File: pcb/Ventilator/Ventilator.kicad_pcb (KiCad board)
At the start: 2 copper layers, 68 parts, among them J1 Screw_Terminal_01x08, J2 Screw_Terminal_01x02, J3 Screw_Terminal_01x08, K1 FINDER-40.52.7.012.0000, K2 FINDER-40.52.7.012.0000, K3 FINDER-40.52.7.012.0000, Q1 NUD3160, Q2 NUD3160, Q3 NUD3160, SW1 Reset, U1 4N25, U2 4N25, U3 4N25, U4 4N25

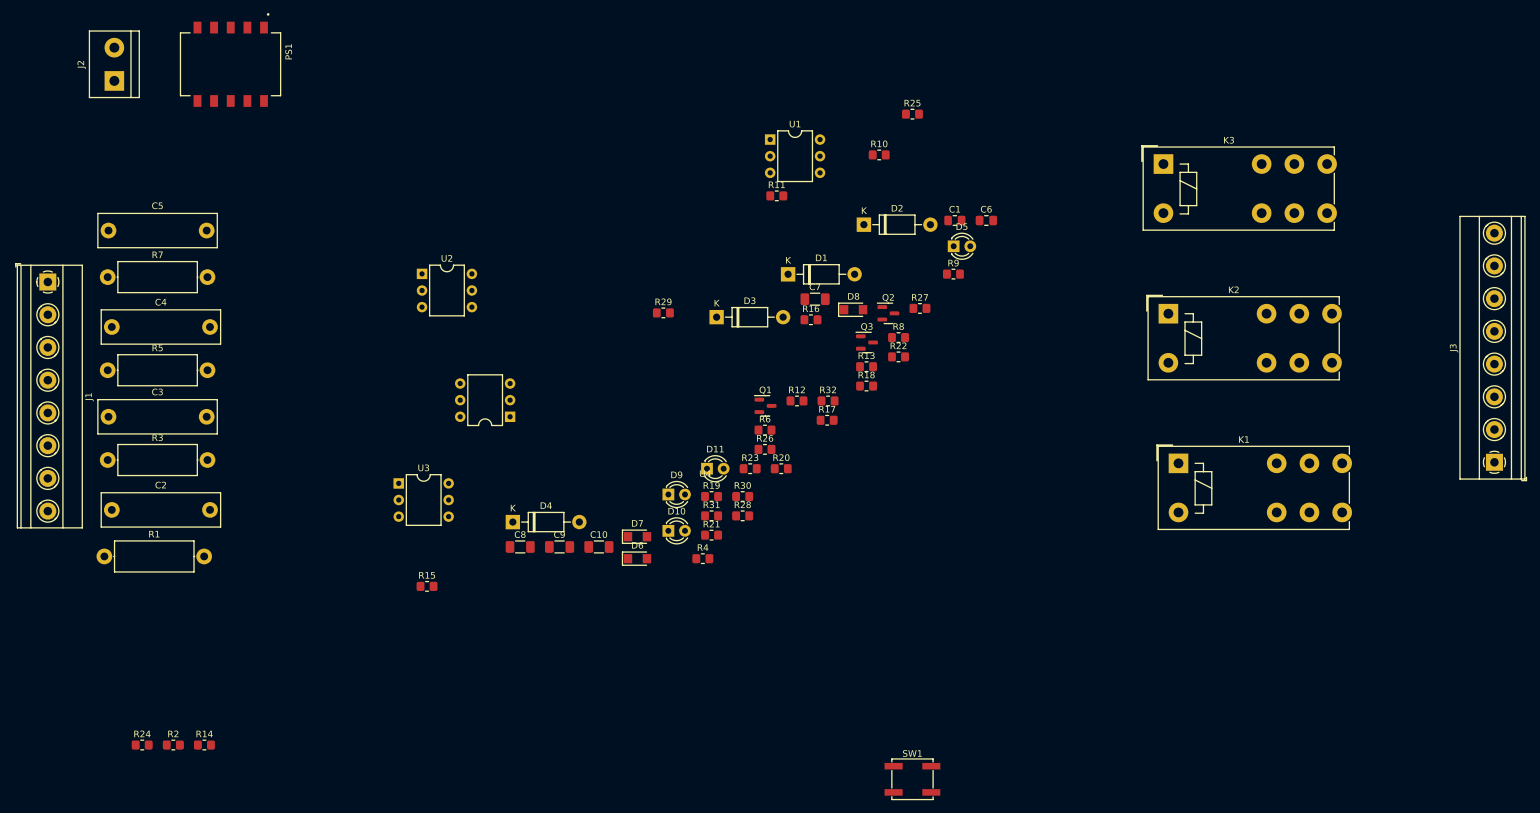
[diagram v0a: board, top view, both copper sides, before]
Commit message: -components placed
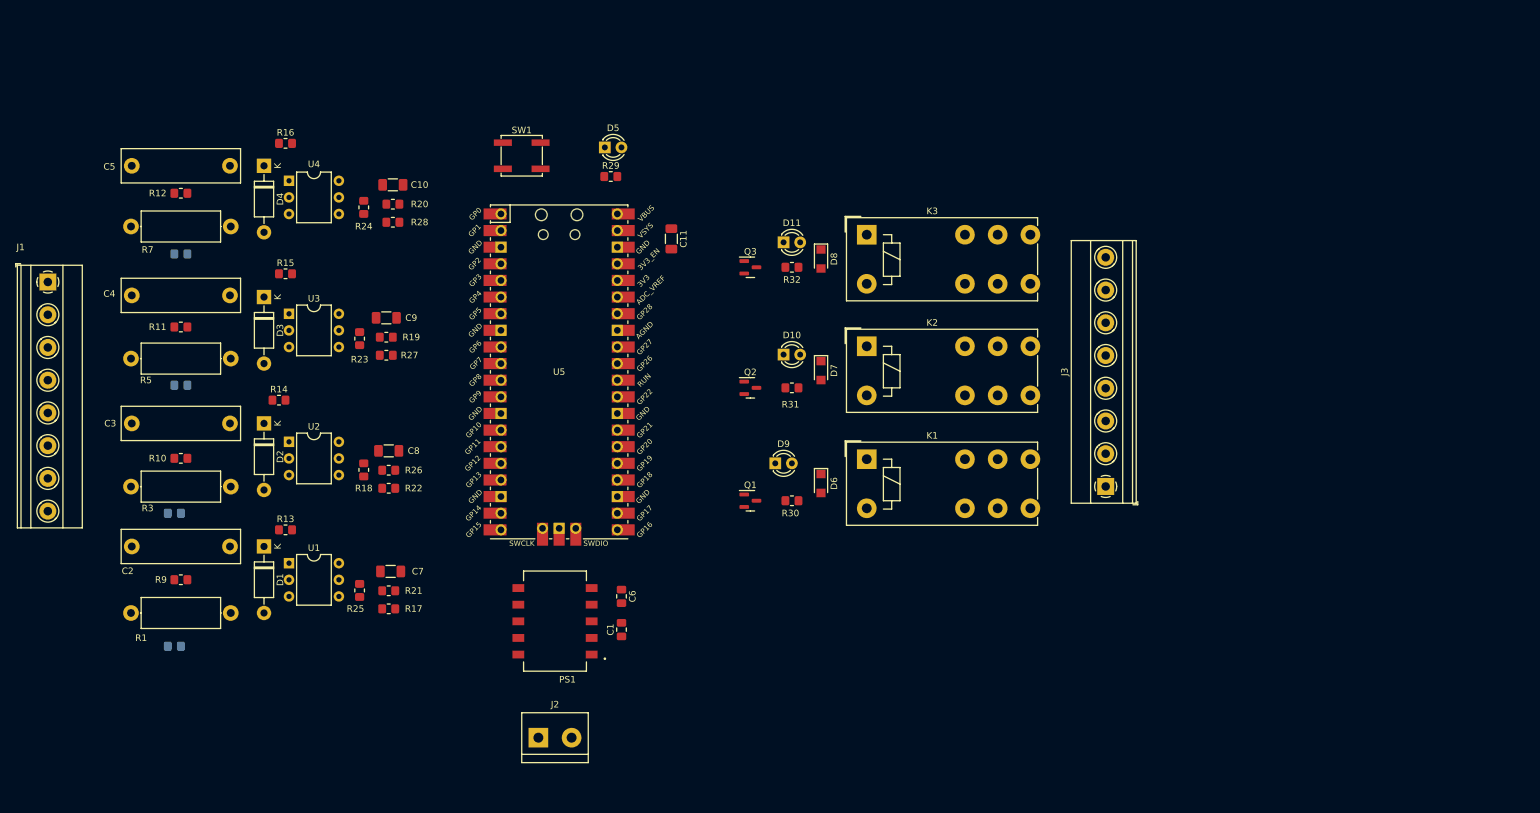
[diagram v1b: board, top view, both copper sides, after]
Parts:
- added C11: 100n, Capacitor_SMD:C_1206_3216Metric_Pad1.33x1.80mm_HandSolder, F.Cu at (118.1, 67.3)
- added U5: Pico, MCU_RaspberryPi_and_Boards:RPi_Pico_SMD_TH, F.Cu at (101.0, 87.6)
- R2, R4, R6, R8: moved to B.Cu
- moved R9 126.9 mm to (43.2, 119.4), turned to 180 degrees
- moved J2 119.4 mm to (97.8, 143.5), turned to 0 degrees
- moved R10 116.3 mm to (43.2, 100.8), turned to 180 degrees
- moved SW1 112.4 mm to (95.2, 54.6)
- moved R25 111.5 mm to (70.5, 121.0), turned to 90 degrees
- moved R8 110.4 mm to (43.2, 69.6)
- moved R12 99.3 mm to (43.2, 60.3), turned to 180 degrees
- moved PS1 98.5 mm to (100.3, 125.7), turned to 180 degrees
- moved U1 97.9 mm to (59.7, 116.9)
- moved D2 96.5 mm to (55.9, 95.5), turned to -90 degrees
- moved R11 93.2 mm to (43.2, 80.8), turned to 180 degrees
- moved R13 92.2 mm to (59.2, 111.8)
- moved D1 90.2 mm to (55.9, 114.3), turned to -90 degrees
- moved R6 89.5 mm to (43.2, 89.7)
- moved R24 88.8 mm to (71.1, 62.5), turned to 90 degrees
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
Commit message: - as send to JCLPCB
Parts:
- added TP1: TestPoint, TestPoint:TestPoint_Bridge_Pitch2.54mm_Drill1.0mm, F.Cu at (77.5, 127.0)
- added TP2: TestPoint, TestPoint:TestPoint_Bridge_Pitch2.54mm_Drill1.0mm, F.Cu at (77.5, 108.2)
- added TP3: TestPoint, TestPoint:TestPoint_Bridge_Pitch2.54mm_Drill1.0mm, F.Cu at (77.5, 88.4)
- added TP4: TestPoint, TestPoint:TestPoint_Bridge_Pitch2.54mm_Drill1.0mm, F.Cu at (77.5, 68.1)
- moved J2 17.8 mm to (82.8, 133.9)
- moved R25 5.38 mm to (75.1, 123.8), turned to 0 degrees
- moved R22 5.18 mm to (70.7, 102.4), turned to 90 degrees
- moved R21 4.57 mm to (70.4, 120.9), turned to 90 degrees
- moved R18 3.82 mm to (74.9, 102.4), turned to 0 degrees
- moved R17 2.80 mm to (75.1, 121.0)
- moved R26 2.50 mm to (74.9, 105.2)
- moved D9 1.37 mm to (135.1, 102.4)
- moved C7 0.15 mm to (75.1, 118.1)
- turned C8 to 0 degrees
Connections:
- net Net-(R27-Pad2) renamed /IN3
- R25 pad 2: Net-(R25-Pad2) -> /IN1
- R26 pad 2: Net-(R26-Pad2) -> /IN2
- R28 pad 2: Net-(R28-Pad2) -> /IN4
- U5 pad 1: Net-(R25-Pad2) -> Net-(D5-Pad1)
- U5 pad 19: unconnected-(U5-Pad19) -> /IN2
- U5 pad 2: Net-(R26-Pad2) -> /IN4
- U5 pad 20: unconnected-(U5-Pad20) -> /IN1
- U5 pad 21: Net-(Q3-Pad1) -> unconnected-(U5-Pad21)
- U5 pad 22: Net-(Q2-Pad1) -> unconnected-(U5-Pad22)
- U5 pad 29: unconnected-(U5-Pad29) -> Net-(Q2-Pad1)
- U5 pad 34: unconnected-(U5-Pad34) -> Net-(Q3-Pad1)
- U5 pad 5: Net-(R28-Pad2) -> unconnected-(U5-Pad5)
- U5 pad 6: Net-(D5-Pad1) -> unconnected-(U5-Pad6)
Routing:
- net VCC: track 0.00 -> 328.8 mm, vias 0 -> 3
- net Net-(SW1-Pad2): track 0.00 -> 56.0 mm, vias 0 -> 2
- net Net-(R2-Pad1): track 0.00 -> 36.1 mm
- net /IN3: track 0.00 -> 31.6 mm
- net Net-(R4-Pad1): track 0.00 -> 28.8 mm
- net /IN1: track 0.00 -> 27.3 mm
- net Net-(J3-Pad6): track 0.00 -> 27.2 mm
- net Net-(C1-Pad1): track 0.00 -> 26.5 mm
- net /IN2: track 0.00 -> 24.1 mm
- net Net-(Q3-Pad1): track 0.00 -> 22.8 mm
- net Net-(R7-Pad1): track 0.00 -> 22.7 mm
- net Net-(D6-Pad2): track 0.00 -> 22.7 mm
- net Net-(D2-Pad2): track 0.00 -> 22.4 mm
- net /IN4: track 0.00 -> 22.3 mm
- net Net-(R6-Pad1): track 0.00 -> 21.8 mm
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- added copper zone on B.Cu, net GND
- added copper zone on F.Cu, net GND
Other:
- board outline added: 172.7 x 91.4 mm

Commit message: - added rp2040, multiple sheets, etc...
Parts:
- removed J1: Screw_Terminal_01x08, TerminalBlock_Phoenix:TerminalBlock_Phoenix_MKDS-1,5-8_1x08_P5.00mm_Horizontal
- removed R1: 2.2k, Resistor_THT:R_Axial_DIN0414_L11.9mm_D4.5mm_P15.24mm_Horizontal
- removed R2: 100R, Resistor_SMD:R_0805_2012Metric_Pad1.20x1.40mm_HandSolder
- added C12: 100n, Capacitor_SMD:C_1206_3216Metric_Pad1.33x1.80mm_HandSolder, F.Cu at (158.6, 138.7)
- added C13: 100n, Capacitor_SMD:C_1206_3216Metric_Pad1.33x1.80mm_HandSolder, F.Cu at (158.6, 142.0)
- added C14: 100n, Capacitor_SMD:C_1206_3216Metric_Pad1.33x1.80mm_HandSolder, F.Cu at (170.6, 135.3)
- added C15: 0.1u, Capacitor_THT:C_Rect_L18.0mm_W5.0mm_P15.00mm_FKS3_FKP3, F.Cu at (83.0, 84.5)
- added C16: 0.1u, Capacitor_THT:C_Rect_L18.0mm_W5.0mm_P15.00mm_FKS3_FKP3, F.Cu at (63.5, 91.1)
- added C17: 100u, Capacitor_SMD:C_1206_3216Metric_Pad1.33x1.80mm_HandSolder, F.Cu at (116.5, 87.0)
- added C18: 100u, Capacitor_SMD:C_1206_3216Metric_Pad1.33x1.80mm_HandSolder, F.Cu at (139.7, 71.0)
- added C19: 0.1u, Capacitor_THT:C_Rect_L18.0mm_W5.0mm_P15.00mm_FKS3_FKP3, F.Cu at (63.5, 84.5)
- added C20: 0.1u, Capacitor_THT:C_Rect_L18.0mm_W5.0mm_P15.00mm_FKS3_FKP3, F.Cu at (105.5, 72.7)
- added C21: 100u, Capacitor_SMD:C_1206_3216Metric_Pad1.33x1.80mm_HandSolder, F.Cu at (116.5, 83.7)
- added C22: 100u, Capacitor_SMD:C_1206_3216Metric_Pad1.33x1.80mm_HandSolder, F.Cu at (84.7, 112.4)
- added C23: 10u, Capacitor_SMD:C_0805_2012Metric_Pad1.18x1.45mm_HandSolder, F.Cu at (180.7, 70.9)
- added C24: 22u, Capacitor_SMD:C_0805_2012Metric_Pad1.18x1.45mm_HandSolder, F.Cu at (175.9, 73.9)
- added C25: 10u, Capacitor_SMD:C_0805_2012Metric_Pad1.18x1.45mm_HandSolder, F.Cu at (175.9, 70.9)
- added C26: 10u, Capacitor_SMD:C_0805_2012Metric_Pad1.18x1.45mm_HandSolder, F.Cu at (174.2, 79.9)
- added J4: Screw_Terminal_01x02, TerminalBlock:TerminalBlock_bornier-2_P5.08mm, F.Cu at (165.1, 73.9)
- added R33: 5k1, Resistor_SMD:R_0805_2012Metric_Pad1.20x1.40mm_HandSolder, F.Cu at (115.1, 128.9)
- added R34: 5k1, Resistor_SMD:R_0805_2012Metric_Pad1.20x1.40mm_HandSolder, F.Cu at (105.6, 128.9)
- added U6: 4N25, Package_DIP:DIP-6_W7.62mm, F.Cu at (92.9, 99.1)
- added U7: NCP1117-3.3_SOT223, Package_TO_SOT_SMD:SOT-223-3_TabPin2, F.Cu at (166.8, 82.5)
- C1: value 10u -> 100n; footprint Capacitor_SMD:C_0805_2012Metric_Pad1.18x1.45mm_HandSolder -> Capacitor_SMD:C_1206_3216Metric_Pad1.33x1.80mm_HandSolder
- C10, C8, C9: value 100u -> 100n
- C2, C3: value 0.1u -> 22p; footprint Capacitor_THT:C_Rect_L18.0mm_W5.0mm_P15.00mm_FKS3_FKP3 -> Capacitor_SMD:C_1206_3216Metric_Pad1.33x1.80mm_HandSolder
- C4: value 0.1u -> 1u; footprint Capacitor_THT:C_Rect_L18.0mm_W5.0mm_P15.00mm_FKS3_FKP3 -> Capacitor_SMD:C_1206_3216Metric_Pad1.33x1.80mm_HandSolder
- C5: value 0.1u -> 100n; footprint Capacitor_THT:C_Rect_L18.0mm_W5.0mm_P15.00mm_FKS3_FKP3 -> Capacitor_SMD:C_1206_3216Metric_Pad1.33x1.80mm_HandSolder
- C6: value 22u -> 100n; footprint Capacitor_SMD:C_0805_2012Metric_Pad1.18x1.45mm_HandSolder -> Capacitor_SMD:C_1206_3216Metric_Pad1.33x1.80mm_HandSolder
- C7: value 100u -> 1u
- D1: value 1N4007 -> LED; footprint Diode_THT:D_DO-41_SOD81_P10.16mm_Horizontal -> LED_THT:LED_D3.0mm
- D5: value LED -> 1N4007; footprint LED_THT:LED_D3.0mm -> Diode_THT:D_DO-41_SOD81_P10.16mm_Horizontal
- J2: value Screw_Terminal_01x02 -> Screw_Terminal_01x08; footprint TerminalBlock:TerminalBlock_bornier-2_P5.08mm -> TerminalBlock_Phoenix:TerminalBlock_Phoenix_MKDS-1,5-8_1x08_P5.00mm_Horizontal
- R10, R11: value 470k -> 220R
- R12: value 470k -> 17k
- R13: value 220R -> 17k
- R14, R15: value 220R -> 6R2
- R16: value 220R -> 10k
- R17: value 17k -> 10k
- R18, R20: value 17k -> 2k2; footprint Resistor_SMD:R_0805_2012Metric_Pad1.20x1.40mm_HandSolder -> Resistor_THT:R_Axial_DIN0414_L11.9mm_D4.5mm_P15.24mm_Horizontal
- R19: value 17k -> 100R
- R21: value 6R2 -> 100R
- R22, R23: value 6R2 -> 470k
- R24: value 6R2 -> 220R
- R25: value 10k -> 220R
- R26, R27: value 10k -> 17k
- R28, R29: value R -> 6R2
- R3: value 2k2 -> 750R; footprint Resistor_THT:R_Axial_DIN0414_L11.9mm_D4.5mm_P15.24mm_Horizontal -> Resistor_SMD:R_0805_2012Metric_Pad1.20x1.40mm_HandSolder
- R30, R31: value R -> 10k
- R32: value R -> 5k1
- R4: value 100R -> 2.2k; footprint Resistor_SMD:R_0805_2012Metric_Pad1.20x1.40mm_HandSolder -> Resistor_THT:R_Axial_DIN0414_L11.9mm_D4.5mm_P15.24mm_Horizontal; moved to F.Cu
- R5, R7: value 2k2 -> 100R; footprint Resistor_THT:R_Axial_DIN0414_L11.9mm_D4.5mm_P15.24mm_Horizontal -> Resistor_SMD:R_0805_2012Metric_Pad1.20x1.40mm_HandSolder
- R6: value 100R -> 2k2; footprint Resistor_SMD:R_0805_2012Metric_Pad1.20x1.40mm_HandSolder -> Resistor_THT:R_Axial_DIN0414_L11.9mm_D4.5mm_P15.24mm_Horizontal; moved to F.Cu
- R8: value 100R -> 470k; moved to F.Cu
- U1: value 4N25 -> W25Q128JVS; footprint Package_DIP:DIP-6_W7.62mm -> Package_SO:SOIC-8_5.23x5.23mm_P1.27mm
- U2: value 4N25 -> RP2040; footprint Package_DIP:DIP-6_W7.62mm -> Package_DFN_QFN:QFN-56-1EP_7x7mm_P0.4mm_EP3.2x3.2mm
- U5: value Pico -> 4N25; footprint MCU_RaspberryPi_and_Boards:RPi_Pico_SMD_TH -> Package_DIP:DIP-6_W7.62mm
- moved C5 140.7 mm to (164.6, 138.7), turned to 0 degrees
- moved J3 121.3 mm to (64.7, 124.8), turned to 0 degrees
- moved C10 113.2 mm to (152.6, 142.0)
- moved D1 112.9 mm to (168.6, 121.3), turned to 0 degrees
- moved R3 112.3 mm to (145.6, 127.6)
- moved C3 107.1 mm to (154.9, 120.3), turned to 0 degrees
- moved K3 106.6 mm to (65.1, 133.8)
- moved U2 105.5 mm to (162.2, 123.2)
- moved C4 105.4 mm to (140.2, 131.6), turned to 0 degrees
- moved C2 104.3 mm to (154.9, 117.0), turned to 0 degrees
- moved C9 98.0 mm to (152.6, 138.7)
- moved K1 95.3 mm to (65.1, 147.9)
- moved C7 91.2 mm to (164.6, 135.3)
- moved R9 89.6 mm to (126.6, 86.6), turned to 0 degrees
- moved SW1 88.7 mm to (152.6, 122.3)
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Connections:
- C1 pad 1: Net-(C1-Pad1) -> unconnected-(C1-Pad1)
- C1 pad 2: GND -> unconnected-(C1-Pad2)
- C10 pad 1: Net-(C10-Pad1) -> +3.3V
- C11 pad 1: VCC -> +3.3V
- C2 pad 2: Net-(C2-Pad2) -> GND
- C3 pad 2: Net-(C3-Pad2) -> GND
- C4 pad 2: Net-(C4-Pad2) -> GND
- C5 pad 1: Net-(C5-Pad1) -> GND
- C5 pad 2: Net-(C5-Pad2) -> Net-(C4-Pad1)
- C6 pad 1: VCC -> GND
- C6 pad 2: GND -> Net-(C4-Pad1)
- C7 pad 1: Net-(C7-Pad1) -> +3.3V
- C8 pad 1: Net-(C8-Pad1) -> +3.3V
- C9 pad 1: Net-(C9-Pad1) -> +3.3V
- D1 pad 1: Net-(C2-Pad1) -> Net-(D1-Pad1)
- D2 pad 1: Net-(C3-Pad1) -> Net-(C15-Pad1)
- D3 pad 1: Net-(C4-Pad1) -> Net-(C16-Pad1)
- D4 pad 1: Net-(C5-Pad1) -> Net-(C19-Pad1)
- D5 pad 1: Net-(D5-Pad1) -> Net-(C20-Pad1)
- J2 pad 1: GND -> /Input/SCT8
- J2 pad 2: Net-(C1-Pad1) -> /Input/SCT7
- PS1 pad 1: Net-(C1-Pad1) -> Net-(C23-Pad1)
- PS1 pad 2: Net-(C1-Pad1) -> Net-(C23-Pad1)
- Q1 pad 1: Net-(Q1-Pad1) -> /CPU/OUT1
- Q2 pad 1: Net-(Q2-Pad1) -> /CPU/OUT3
- Q3 pad 1: Net-(Q3-Pad1) -> /CPU/OUT2
- R10 pad 1: Net-(C3-Pad1) -> Net-(C15-Pad1)
- R10 pad 2: Net-(C3-Pad2) -> Net-(R10-Pad2)
- R11 pad 1: Net-(C4-Pad1) -> Net-(C16-Pad1)
- R11 pad 2: Net-(C4-Pad2) -> Net-(R11-Pad2)
- R12 pad 1: Net-(C5-Pad1) -> Net-(R12-Pad1)
- R12 pad 2: Net-(C5-Pad2) -> GND
- R13 pad 1: Net-(C2-Pad1) -> Net-(R13-Pad1)
- R13 pad 2: Net-(R13-Pad2) -> GND
- R14 pad 1: Net-(C3-Pad1) -> Net-(R12-Pad1)
- R14 pad 2: Net-(R14-Pad2) -> Net-(C17-Pad1)
- R15 pad 1: Net-(C4-Pad1) -> Net-(R13-Pad1)
- R15 pad 2: Net-(R15-Pad2) -> Net-(C18-Pad1)
- R16 pad 1: Net-(C5-Pad1) -> Net-(R12-Pad1)
- R16 pad 2: Net-(R16-Pad2) -> /CPU/IN1
- R17 pad 1: Net-(R17-Pad1) -> Net-(R13-Pad1)
- R17 pad 2: GND -> /CPU/IN3
- R18 pad 1: Net-(R18-Pad1) -> /Input/SCT7
- R18 pad 2: GND -> Net-(C19-Pad2)
- R19 pad 1: Net-(R19-Pad1) -> /Input/SCT8
- R19 pad 2: GND -> Net-(D4-Pad2)
- R20 pad 1: Net-(R20-Pad1) -> /Input/SCT3
- R20 pad 2: GND -> Net-(C20-Pad2)
- R21 pad 1: Net-(R17-Pad1) -> /Input/SCT4
- R21 pad 2: Net-(C7-Pad1) -> Net-(D5-Pad2)
- R22 pad 1: Net-(R18-Pad1) -> Net-(C19-Pad1)
- R22 pad 2: Net-(C8-Pad1) -> Net-(C19-Pad2)
- R23 pad 1: Net-(R19-Pad1) -> Net-(C20-Pad1)
- R23 pad 2: Net-(C9-Pad1) -> Net-(C20-Pad2)
- R24 pad 1: Net-(R20-Pad1) -> Net-(C19-Pad1)
- R24 pad 2: Net-(C10-Pad1) -> Net-(R24-Pad2)
- R25 pad 1: Net-(R17-Pad1) -> Net-(C20-Pad1)
- R25 pad 2: /IN1 -> Net-(R25-Pad2)
- R26 pad 1: Net-(R18-Pad1) -> Net-(R26-Pad1)
- R26 pad 2: /IN2 -> GND
- R27 pad 1: Net-(R19-Pad1) -> Net-(R27-Pad1)
- R27 pad 2: /IN3 -> GND
- R28 pad 1: Net-(R20-Pad1) -> Net-(R26-Pad1)
- R28 pad 2: /IN4 -> Net-(C21-Pad1)
- R29 pad 1: VCC -> Net-(R27-Pad1)
- R29 pad 2: Net-(D5-Pad2) -> Net-(C22-Pad1)
- R3 pad 1: Net-(J1-Pad6) -> Net-(D1-Pad2)
- R3 pad 2: Net-(C3-Pad2) -> VCC
- R30 pad 1: Net-(D9-Pad1) -> Net-(R26-Pad1)
- R30 pad 2: Net-(D6-Pad2) -> /CPU/IN4
- R31 pad 1: Net-(D10-Pad1) -> Net-(R27-Pad1)
- R31 pad 2: Net-(D7-Pad2) -> /CPU/IN2
- R32 pad 1: Net-(D11-Pad1) -> Net-(D9-Pad1)
- R32 pad 2: Net-(D8-Pad2) -> Net-(D6-Pad2)
- R4 pad 1: Net-(R4-Pad1) -> /Input/SCT1
- R4 pad 2: Net-(D2-Pad2) -> Net-(C15-Pad2)
- R5 pad 1: Net-(R5-Pad1) -> /Input/SCT2
- R5 pad 2: Net-(C4-Pad2) -> Net-(D2-Pad2)
- R6 pad 1: Net-(R6-Pad1) -> /Input/SCT5
- R6 pad 2: Net-(D3-Pad2) -> Net-(C16-Pad2)
- R7 pad 1: Net-(R7-Pad1) -> /Input/SCT6
- R7 pad 2: Net-(C5-Pad2) -> Net-(D3-Pad2)
- R8 pad 1: Net-(R8-Pad1) -> Net-(C15-Pad1)
- R8 pad 2: Net-(D4-Pad2) -> Net-(C15-Pad2)
- R9 pad 1: Net-(C2-Pad1) -> Net-(C16-Pad1)
- R9 pad 2: Net-(C2-Pad2) -> Net-(C16-Pad2)
- SW1 pad 2: Net-(SW1-Pad2) -> Net-(R2-Pad1)
- TP1 pad 1: /IN1 -> /CPU/IN1
- TP2 pad 1: /IN2 -> /CPU/IN3
- TP3 pad 1: /IN3 -> /CPU/IN4
- TP4 pad 1: /IN4 -> /CPU/IN2
- U1 pad 1: Net-(R13-Pad2) -> Net-(U1-Pad1)
- U1 pad 2: Net-(D1-Pad2) -> Net-(U1-Pad2)
- U1 pad 3: unconnected-(U1-Pad3) -> Net-(U1-Pad3)
- U1 pad 4: Net-(R17-Pad1) -> GND
- U1 pad 5: VCC -> Net-(U1-Pad5)
- U1 pad 6: unconnected-(U1-Pad6) -> Net-(U1-Pad6)
- U2 pad 1: Net-(R14-Pad2) -> +3.3V
- U2 pad 2: Net-(D2-Pad2) -> unconnected-(U2-Pad2)
- U2 pad 4: Net-(R18-Pad1) -> Net-(D1-Pad1)
- U2 pad 5: VCC -> /CPU/IN1
- U2 pad 6: unconnected-(U2-Pad6) -> /CPU/IN2
- U3 pad 1: Net-(R15-Pad2) -> Net-(R10-Pad2)
- U3 pad 2: Net-(D3-Pad2) -> Net-(D2-Pad2)
- U3 pad 4: Net-(R19-Pad1) -> Net-(R12-Pad1)
- U4 pad 1: Net-(R16-Pad2) -> Net-(R11-Pad2)
- U4 pad 2: Net-(D4-Pad2) -> Net-(D3-Pad2)
- U4 pad 4: Net-(R20-Pad1) -> Net-(R13-Pad1)
- U5 pad 1: Net-(D5-Pad1) -> Net-(R24-Pad2)
- U5 pad 2: /IN4 -> Net-(D4-Pad2)
- U5 pad 3: GND -> unconnected-(U5-Pad3)
- U5 pad 4: /IN3 -> Net-(R26-Pad1)
- U5 pad 5: unconnected-(U5-Pad5) -> VCC
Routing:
- net VCC: track 328.8 -> 0.00 mm, vias 3 -> 0
- net Net-(SW1-Pad2): track 56.0 -> 0.00 mm, vias 2 -> 0
- net Net-(R2-Pad1): track 36.1 -> 0.00 mm
- net /IN3: track 31.6 -> 0.00 mm
- net Net-(R4-Pad1): track 28.8 -> 0.00 mm
- net /IN1: track 27.3 -> 0.00 mm
- net Net-(J3-Pad6): track 27.2 -> 0.00 mm
- net Net-(C1-Pad1): track 26.5 -> 0.00 mm
- net /IN2: track 24.1 -> 0.00 mm
- net Net-(Q3-Pad1): track 22.8 -> 0.00 mm
- net Net-(R7-Pad1): track 22.7 -> 0.00 mm
- net Net-(D6-Pad2): track 22.7 -> 0.00 mm
- net Net-(D2-Pad2): track 22.4 -> 0.00 mm
- net /IN4: track 22.3 -> 0.00 mm
- net Net-(R6-Pad1): track 21.8 -> 0.00 mm
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- removed copper zone on B.Cu, net GND
- removed copper zone on F.Cu, net GND
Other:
- board outline removed
